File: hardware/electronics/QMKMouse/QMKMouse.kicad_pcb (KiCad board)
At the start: 4 copper layers, 104.6 x 65.8 mm, 117 parts

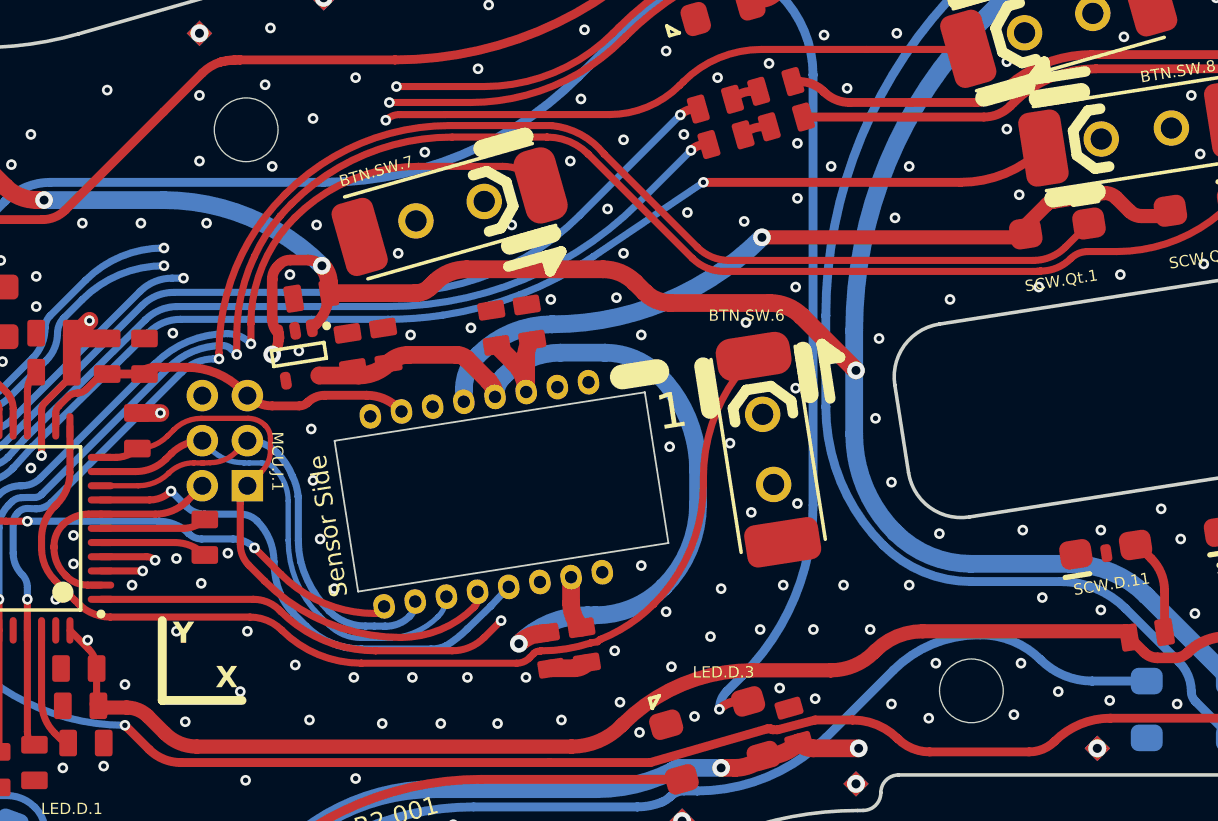
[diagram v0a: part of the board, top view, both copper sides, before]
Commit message: update schematic from PCB; sync netlist and fix some symbol orientations; also fix LED symbol
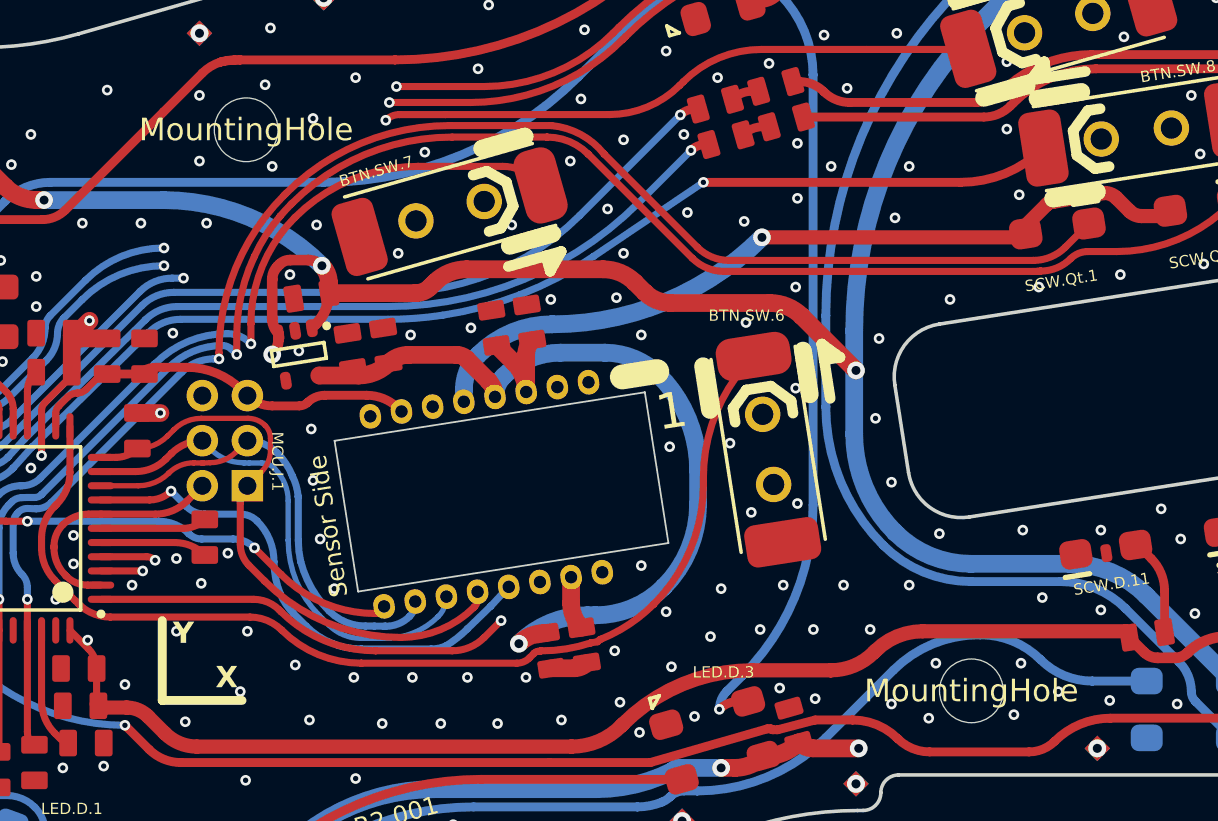
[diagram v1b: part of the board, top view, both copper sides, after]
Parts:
- BTN.SW.7, BTN.SW.8: value D2LS-21 -> SW_DIP_x01
- HOLE.1, HOLE.2: value (none) -> MountingHole
- LED.C.20, LED.C.21, LED.C.23, LED.C.24, LED.C.25, LED.C.26, LED.C.27, LED.C.28, MCU.C.22, MCU.C.4, MCU.C.5, MCU.C.6, MCU.C.8, MCU.C.9: value 0805 -> 0.1uF 100V
- LED.D.5: value IN-PI55TATPRPGPB -> Inolux_IN-PI554FCH
- LED.R.16, LED.R.17, LED.R.18, LED.R.19, SCW.R.2, SCW.R.4: value 0805 -> 1k 1%
- MCH.FID.1, MCH.FID.2: value IPC-7351 Fiducial 1mm -> Fiducial
- MCH.LOGO.2: value Coordinate system marker for assembly -> Coordinate_system_marker
- MCH.SP.1, MCH.SP.10, MCH.SP.11, MCH.SP.12, MCH.SP.13, MCH.SP.14, MCH.SP.15, MCH.SP.16, MCH.SP.17, MCH.SP.18, MCH.SP.19, MCH.SP.2, MCH.SP.20, MCH.SP.21, MCH.SP.22, MCH.SP.23, MCH.SP.24, MCH.SP.25, MCH.SP.26, MCH.SP.27, MCH.SP.28, MCH.SP.3, MCH.SP.4, MCH.SP.5, MCH.SP.6, MCH.SP.7, MCH.SP.8, MCH.SP.9: value Spark Gap -> Spark_gap
- MCU.C.1, REG.C.12, REG.C.14, REG.C.16, REG.C.18: value 0805 -> 1uF 25V
- MCU.C.7, MOS.C.10, MOS.C.11, REG.C.13, REG.C.17, USB.C.19: value 0805 -> 10uF 25V
- MCU.J.4: value HEADER2 -> Conn_01x02
- MCU.R.1, MCU.R.20, MOS.R.5, USB.R.12, USB.R.13, USB.R.14, USB.R.15, USB.R.8, USB.R.9: value 0805 -> 10k 1%
- MCU.U.1: value ATMEGA32U4RC-AU -> ATmega32U4RC-A
- MCU.Y.1: value LFXTAL055663BULK -> 8MHz
- MOS.R.3, MOS.R.4, USB.R.6, USB.R.7: value 0805 -> 22R 1%
- REG.C.15: value 0805 -> 100pF 100V
- SCW.D.11, SCW.D.12: value IR12-21C/TR8 or VSMB10940 -> IR12-21C/TR8 or VSMB10940
- SCW.R.1, SCW.R.3: value 0805 -> 100 1%
- USB.FB.4: value ACML-0805-601-T -> ACML-0805-601-T Ferrite Bead 600Ohm
- USB.R.10, USB.R.11: value 0805 -> 100R 1%
- USB.Z.1: value IP4220CZ6,125 -> IP4220CZ6
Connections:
- net NetLED.D.1_2 renamed Net-(LED.D.1-Pad2)
- net NetLED.D.1_4 renamed Net-(LED.D.1-Pad4)
- net NetLED.D.2_2 renamed Net-(LED.D.2-Pad2)
- net NetLED.D.2_4 renamed Net-(LED.D.2-Pad4)
- net NetLED.D.3_2 renamed Net-(LED.D.3-Pad2)
- net NetLED.D.4_2 renamed Net-(LED.D.4-Pad2)
- net NetLED.D.5_2 renamed Net-(LED.D.5-Pad2)
- net NetLED.D.6_2 renamed Net-(LED.D.6-Pad2)
- net NetLED.D.7_2 renamed Net-(LED.D.7-Pad2)
- net NetLED.D.8_2 renamed Net-(LED.D.8-Pad2)
- net NetMCU.C.4_2 renamed Net-(MCU.C.4-Pad2)
- net NetMCU.J.4_1 renamed Net-(MCU.J.4-Pad1)
- net NetMCU.U.1_16 renamed Net-(MCU.U.1-Pad16)
- net NetMCU.U.1_17 renamed Net-(MCU.U.1-Pad17)
- net NetMCU.U.1_18 renamed SCL
- net NetMCU.U.1_19 renamed SDA
- net NetMCU.U.1_21 renamed MOTION
- net NetMCU.U.1_3 renamed D-
- net NetMCU.U.1_4 renamed D+
- net NetMOS.C.10_2 renamed Net-(MOS.C.10-Pad2)
- net NetMOS.R.3_1 renamed Net-(MOS.R.3-Pad1)
- net NetMOS.R.4_1 renamed Net-(MOS.R.4-Pad1)
- net NetREG.C.15_2 renamed Net-(REG.C.15-Pad2)
- net NetUSB.FB.2_1 renamed Net-(USB.FB.2-Pad1)
- net NetUSB.FB.2_2 renamed Net-(USB.FB.2-Pad2)
- net NetUSB.FB.3_1 renamed Net-(USB.FB.3-Pad1)
- net NetUSB.FB.3_2 renamed Net-(USB.FB.3-Pad2)
- net NetUSB.FB.4_1 renamed Net-(USB.FB.4-Pad1)
- net NetUSB.FB.4_2 renamed Net-(USB.FB.4-Pad2)
- net NetUSB.FB.5_1 renamed Net-(USB.FB.5-Pad1)
- net NetUSB.FB.5_2 renamed Net-(USB.FB.5-Pad2)
- net NetUSB.J.3_3 renamed Net-(USB.J.3-Pad3)
- net NetUSB.J.3_9 renamed Net-(USB.J.3-Pad9)
- net ~{CS renamed ~{CS}
- net ~{RESET renamed ~{RESET}
- BTN.SW.3 pad A: NetBTN.SW.3_A -> (no net)
- BTN.SW.3 pad B: GND -> (no net)
- BTN.SW.6 pad A: NetBTN.SW.6_A -> (no net)
- BTN.SW.6 pad B: GND -> (no net)
- BTN.SW.7 pad A: NetBTN.SW.7_A -> (no net)
- BTN.SW.7 pad B: GND -> (no net)
- LBS.SW.2 pad A: NetLBS.SW.2_A -> (no net)
- LBS.SW.2 pad B: GND -> (no net)
- LED.C.25 pad 1: GND -> unconnected-(LED.C.25-Pad1)
- LED.R.18 pad 1: (no net) -> unconnected-(LED.R.18-Pad1)
- LED.R.19 pad 1: (no net) -> unconnected-(LED.R.19-Pad1)
- MCH.SP.1 pad 1: GND -> (no net)
- MCH.SP.10 pad 1: GND -> (no net)
- MCH.SP.11 pad 1: GND -> (no net)
- MCH.SP.12 pad 1: GND -> (no net)
- MCH.SP.13 pad 1: GND -> (no net)
- MCH.SP.14 pad 1: GND -> (no net)
- MCH.SP.15 pad 1: GND -> (no net)
- MCH.SP.16 pad 1: GND -> (no net)
- MCH.SP.17 pad 1: GND -> (no net)
- MCH.SP.18 pad 1: GND -> (no net)
- MCH.SP.19 pad 1: GND -> (no net)
- MCH.SP.2 pad 1: GND -> (no net)
- MCH.SP.20 pad 1: GND -> (no net)
- MCH.SP.21 pad 1: GND -> (no net)
- MCH.SP.22 pad 1: GND -> (no net)
- MCH.SP.23 pad 1: GND -> (no net)
- MCH.SP.24 pad 1: GND -> (no net)
- MCH.SP.25 pad 1: GND -> (no net)
- MCH.SP.26 pad 1: GND -> (no net)
- MCH.SP.27 pad 1: GND -> (no net)
- MCH.SP.28 pad 1: GND -> (no net)
- MCH.SP.3 pad 1: GND -> (no net)
- MCH.SP.4 pad 1: GND -> (no net)
- MCH.SP.5 pad 1: GND -> (no net)
- MCH.SP.6 pad 1: GND -> (no net)
- MCH.SP.7 pad 1: GND -> (no net)
- MCH.SP.8 pad 1: GND -> (no net)
- MCH.SP.9 pad 1: GND -> (no net)
- MCU.C.1 pad 1: GND -> Net-(MCU.C.1-Pad1)
- MCU.C.1 pad 2: NetMCU.C.1_2 -> GND
- MCU.U.1 pad 1: NetLBS.SW.2_A -> ButtonRightClick
- MCU.U.1 pad 12: NetBTN.SW.6_A -> ButtonDPI
- MCU.U.1 pad 20: NetBTN.SW.8_A -> ButtonScrollWheel
- MCU.U.1 pad 22: (no net) -> unconnected-(MCU.U.1-Pad22)
- MCU.U.1 pad 25: NetLBS.SW.1_A -> ButtonLeftClick
- MCU.U.1 pad 27: NetBTN.SW.5_A -> ButtonForward
- MCU.U.1 pad 30: NetBTN.SW.7_A -> ButtonBack
- MCU.U.1 pad 31: NetBTN.SW.3_A -> ButtonRR
- MCU.U.1 pad 32: NetBTN.SW.4_A -> ButtonLL
- MCU.U.1 pad 39: NetMCU.U.1_39 -> TopScrollWheelOpto1
- MCU.U.1 pad 41: NetMCU.U.1_41 -> TopScrollWheelOpto0
- MCU.U.1 pad 6: NetMCU.C.1_2 -> Net-(MCU.C.1-Pad1)
- MOS.U.2 pad 1: (no net) -> unconnected-(MOS.U.2-Pad1)
- MOS.U.2 pad 14: (no net) -> unconnected-(MOS.U.2-Pad14)
- MOS.U.2 pad 16: (no net) -> unconnected-(MOS.U.2-Pad16)
- MOS.U.2 pad 2: (no net) -> unconnected-(MOS.U.2-Pad2)
- MOS.U.2 pad 6: (no net) -> unconnected-(MOS.U.2-Pad6)
- REG.U.4 pad 4: (no net) -> unconnected-(REG.U.4-Pad4)
- SCW.R.1 pad 1: NetSCW.D.11_A -> Net-(SCW.D.11-Pad2)
- SCW.R.2 pad 2: NetMCU.U.1_41 -> TopScrollWheelOpto0
- SCW.R.3 pad 1: NetSCW.D.12_A -> Net-(SCW.D.12-Pad2)
- SCW.R.4 pad 2: NetMCU.U.1_39 -> TopScrollWheelOpto1
- USB.FB.1 pad 1: NetUSB.FB.1_1 -> Net-(USB.FB.1-Pad1)
- USB.J.2 pad 1: NetUSB.FB.1_1 -> Net-(USB.FB.1-Pad1)
- USB.J.3 pad 10: (no net) -> unconnected-(USB.J.3-Pad10)
- USB.J.3 pad 11: NetUSB.FB.1_1 -> (no net)
- USB.J.3 pad 12: GND -> Net-(USB.FB.1-Pad1)
- USB.J.3 pad 2: NetUSB.FB.1_1 -> Net-(USB.FB.1-Pad1)
- USB.J.3 pad 4: (no net) -> unconnected-(USB.J.3-Pad4)
- USB.R.8 pad 2: NetUSB.FB.1_1 -> Net-(USB.FB.1-Pad1)
- USB.R.9 pad 2: NetUSB.FB.1_1 -> Net-(USB.FB.1-Pad1)
- USB.Z.1 pad 5: NetUSB.FB.1_1 -> Net-(USB.FB.1-Pad1)
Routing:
- net NetBTN.SW.4_A: track 106.9 -> 0.00 mm, vias 3 -> 0
- net ButtonLL: track 0.00 -> 106.9 mm, vias 0 -> 3
- net NetBTN.SW.3_A: track 101.5 -> 0.00 mm, vias 2 -> 0
- net ButtonRR: track 0.00 -> 101.5 mm, vias 0 -> 2
- net NetLBS.SW.1_A: track 101.3 -> 0.00 mm, vias 3 -> 0
- net ButtonLeftClick: track 0.00 -> 101.3 mm, vias 0 -> 3
- net TopScrollWheelOpto1: track 0.00 -> 97.4 mm, vias 0 -> 2
- net NetMCU.U.1_39: track 97.4 -> 0.00 mm, vias 2 -> 0
- net NetLBS.SW.2_A: track 89.6 -> 0.00 mm, vias 2 -> 0
- net ButtonRightClick: track 0.00 -> 89.6 mm, vias 0 -> 2
- net TopScrollWheelOpto0: track 0.00 -> 88.2 mm, vias 0 -> 2
- net NetMCU.U.1_41: track 88.2 -> 0.00 mm, vias 2 -> 0
- net NetBTN.SW.5_A: track 71.7 -> 0.00 mm, vias 3 -> 0
- net ButtonForward: track 0.00 -> 71.7 mm, vias 0 -> 3
- net NetBTN.SW.8_A: track 70.2 -> 0.00 mm, vias 2 -> 0
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
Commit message: Fix some schematic PCB mismatch
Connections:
- MCH.SP.1 pad 1: (no net) -> GND
- MCH.SP.10 pad 1: (no net) -> GND
- MCH.SP.11 pad 1: (no net) -> GND
- MCH.SP.12 pad 1: (no net) -> GND
- MCH.SP.13 pad 1: (no net) -> GND
- MCH.SP.14 pad 1: (no net) -> GND
- MCH.SP.15 pad 1: (no net) -> GND
- MCH.SP.16 pad 1: (no net) -> GND
- MCH.SP.17 pad 1: (no net) -> GND
- MCH.SP.18 pad 1: (no net) -> GND
- MCH.SP.19 pad 1: (no net) -> GND
- MCH.SP.2 pad 1: (no net) -> GND
- MCH.SP.20 pad 1: (no net) -> GND
- MCH.SP.21 pad 1: (no net) -> GND
- MCH.SP.22 pad 1: (no net) -> GND
- MCH.SP.23 pad 1: (no net) -> GND
- MCH.SP.24 pad 1: (no net) -> GND
- MCH.SP.25 pad 1: (no net) -> GND
- MCH.SP.26 pad 1: (no net) -> GND
- MCH.SP.27 pad 1: (no net) -> GND
- MCH.SP.28 pad 1: (no net) -> GND
- MCH.SP.3 pad 1: (no net) -> GND
- MCH.SP.4 pad 1: (no net) -> GND
- MCH.SP.5 pad 1: (no net) -> GND
- MCH.SP.6 pad 1: (no net) -> GND
- MCH.SP.7 pad 1: (no net) -> GND
- MCH.SP.8 pad 1: (no net) -> GND
- MCH.SP.9 pad 1: (no net) -> GND
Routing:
- net Net-(MCU.C.1-Pad1): track 6.03 -> 12.0 mm
- net GND: track 9.25 -> 3.27 mm

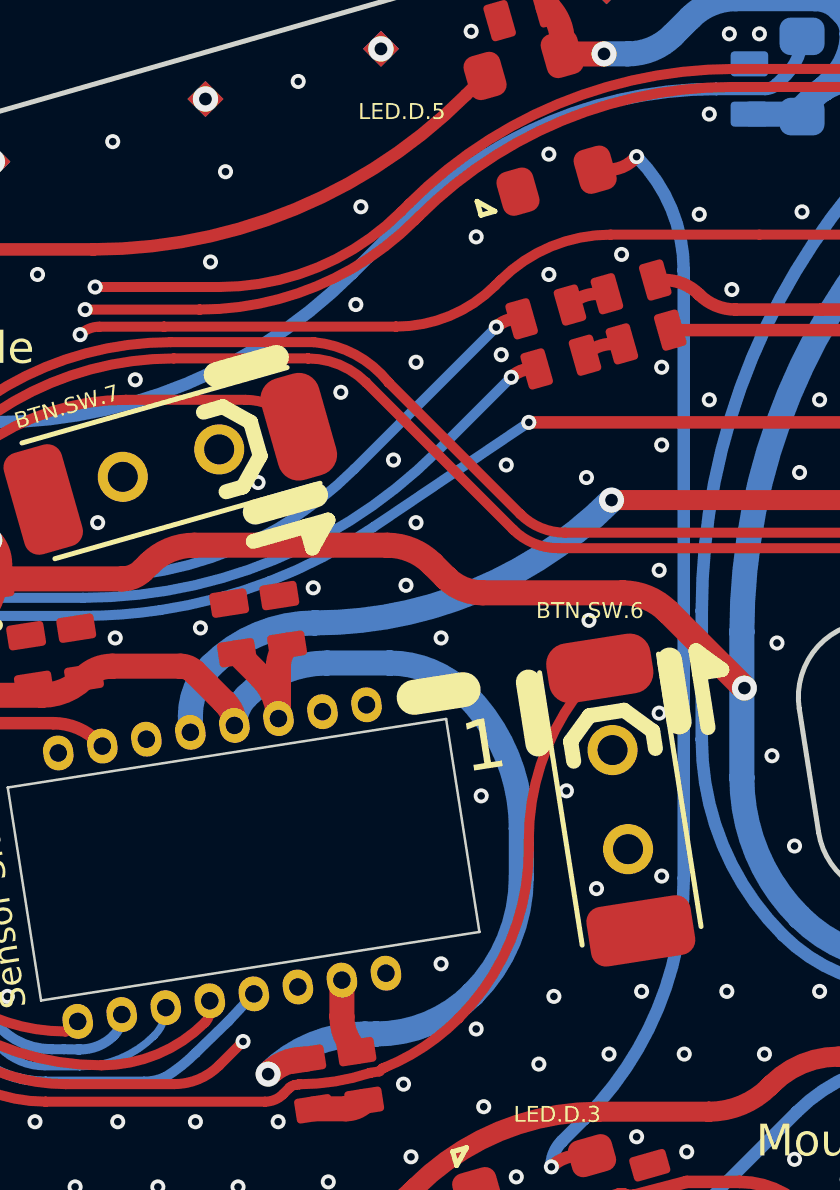
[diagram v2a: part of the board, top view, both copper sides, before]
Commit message: Fix all remaining DRC errors and schematic mismatches
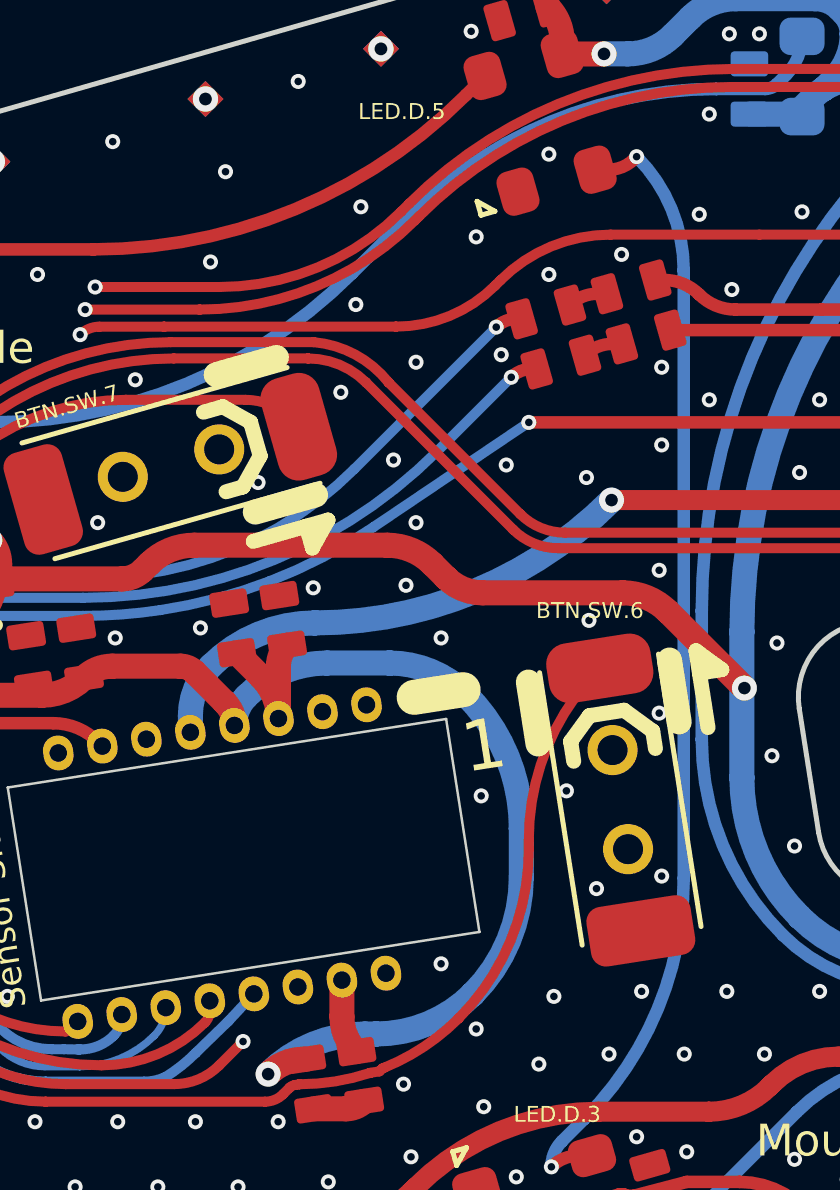
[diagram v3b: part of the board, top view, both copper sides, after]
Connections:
- MCH.FID.1 pad 1: (no net) -> unconnected-(MCH.FID.1-Pad1)
- MCH.FID.2 pad 1: (no net) -> unconnected-(MCH.FID.2-Pad1)
- MCU.C.1 pad 1: Net-(MCU.C.1-Pad1) -> GND
- MCU.C.1 pad 2: GND -> Net-(MCU.C.1-Pad2)
- MCU.U.1 pad 6: Net-(MCU.C.1-Pad1) -> Net-(MCU.C.1-Pad2)
- USB.J.3 pad 11: (no net) -> Net-(USB.FB.1-Pad1)
- USB.J.3 pad 12: Net-(USB.FB.1-Pad1) -> GND
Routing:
- net Net-(MCU.C.1-Pad1): track 12.0 -> 0.00 mm
- net GND: track 3.27 -> 9.30 mm
- net Net-(MCU.C.1-Pad2): track 0.00 -> 5.98 mm

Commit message: fix last sync errors
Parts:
- SCW.D.11, SCW.D.12: footprint LEDs.PcbLib:IR12-21C/TR8 -> LEDs.PcbLib:IR12-21C-TR8
- SCW.Qt.1, SCW.Qt.2: footprint OptoElectronics.PcbLib:PT26-51B/TR8 -> OptoElectronics.PcbLib:PT26-51B-TR8
- turned SCW.D.12 to -81.113 degrees
- turned SCW.Qt.2 to 98.887 degrees
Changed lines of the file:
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@@
     )
   )
-  (footprint "LEDs.PcbLib:IR12-21C{slash}TR8" (layer "F.Cu")
-    (at 179.239409 111.783457 -81.1130838)
+  (footprint "LEDs.PcbLib:IR12-21C-TR8" (layer "F.Cu")
+    (at 179.239409 111.783457 -81.113)
     (property "Sheetfile" "ScrollWheel-SchDoc.kicad_sch")
     (property "Sheetname" "SCW")
-    (fp_text reference "SCW.D.12" (at 2.405868 2.284283 8.8869162 unlocked) (layer "F.SilkS")
-      (effects (font (size 0.635 0.635) (thickness 0.254)) (justify left bottom))
-    )
-    (fp_text value "IR12-21C/TR8 or VSMB10940 " (at 6.000048 1.491927 unlocked) (layer "F.SilkS") hide
+    (fp_text reference "SCW.D.12" (at 2.405868 2.284283 8.887 unlocked) (layer "F.SilkS")
+      (effects (font (size 0.635 0.635) (thickness 0.254)) (justify left bottom))
+    )
+    (fp_text value "IR12-21C/TR8 or VSMB10940 " (at 6.000048 1.491927 8.38e-05 unlocked) (layer "F.SilkS") hide
       (effects (font (size 0.762 0.762) (thickness 0.254)) (justify left bottom))
     )
@@
     (fp_line (start -2.3 1.499999) (end 0.2 1.499999) (layer "B.Fab") (width 0.1))
     (fp_line (start 0.2 1.499999) (end 0.2 -1.5) (layer "B.Fab") (width 0.1))
-    (pad "" smd roundrect locked (at 0.200003 -0.002399 278.8869162) (size 1 0.6) (layers "F.Cu" "F.Paste" "F.Mask") (roundrect_rratio 0.35)
+    (pad "" smd roundrect locked (at 0.200003 -0.002399 278.887) (size 1 0.6) (layers "F.Cu" "F.Paste" "F.Mask") (roundrect_rratio 0.35)
       (solder_paste_margin -99))
-    (pad "1" smd roundrect locked (at 0 1.702397 278.8869162) (size 1.6 1.8) (layers "F.Cu" "F.Paste" "F.Mask") (roundrect_rratio 0.3)
+    (pad "1" smd roundrect locked (at 0 1.702397 278.887) (size 1.6 1.8) (layers "F.Cu" "F.Paste" "F.Mask") (roundrect_rratio 0.3)
       (net 8 "GND") (pinfunction "K") (pintype "passive") (solder_paste_margin -0.03))
-    (pad "2" smd roundrect locked (at 0.000001 -1.702399 278.8869162) (size 1.6 1.8) (layers "F.Cu" "F.Paste" "F.Mask") (roundrect_rratio 0.3)
+    (pad "2" smd roundrect locked (at 0.000001 -1.702399 278.887) (size 1.6 1.8) (layers "F.Cu" "F.Paste" "F.Mask") (roundrect_rratio 0.3)
       (net 35 "Net-(SCW.D.12-Pad2)") (pinfunction "A") (pintype "passive") (solder_paste_margin -0.03))
     (model "${KIPRJMOD}/ALTIUM_EMBEDDED_MODELS/XZxx56x-1.step"
@@
       (net 8 "GND") (pintype "input") (solder_mask_margin 0.1016) (solder_paste_margin -2.5146))
   )
-  (footprint "OptoElectronics.PcbLib:PT26-51B{slash}TR8" (layer "F.Cu")
-    (at 176.514403 93.683425 98.8869162)
+  (footprint "OptoElectronics.PcbLib:PT26-51B-TR8" (layer "F.Cu")
+    (at 176.514403 93.683425 98.887)
     (property "Sheetfile" "ScrollWheel-SchDoc.kicad_sch")
     (property "Sheetname" "SCW")
-    (fp_text reference "SCW.Qt.2" (at -3.298956 -2.338244 8.8869162 unlocked) (layer "F.SilkS")
-      (effects (font (size 0.635 0.635) (thickness 0.254)) (justify left bottom))
-    )
-    (fp_text value "PT26-51B/TR8 or PT12-21B/TR8" (at -3.871855 -2.77779 unlocked) (layer "F.SilkS") hide
+    (fp_text reference "SCW.Qt.2" (at -3.298956 -2.338244 8.887 unlocked) (layer "F.SilkS")
+      (effects (font (size 0.635 0.635) (thickness 0.254)) (justify left bottom))
+    )
+    (fp_text value "PT26-51B/TR8 or PT12-21B/TR8" (at -3.871855 -2.77779 8.38e-05 unlocked) (layer "F.SilkS") hide
       (effects (font (size 0.762 0.762) (thickness 0.254)) (justify left bottom))
     )
@@
     (fp_line (start 0.499999 1.6) (end -2.100007 1.599999) (layer "B.Fab") (width 0.1))
     (fp_line (start 0.5 -1.599999) (end 0.499999 1.6) (layer "B.Fab") (width 0.1))
-    (pad "1" smd roundrect locked (at 0.000001 -1.802398 98.8869162) (size 1.7 1.8) (layers "F.Cu" "F.Paste" "F.Mask") (roundrect_rratio 0.3)
+    (pad "1" smd roundrect locked (at 0.000001 -1.802398 98.887) (size 1.7 1.8) (layers "F.Cu" "F.Paste" "F.Mask") (roundrect_rratio 0.3)
       (net 7 "3V3") (pinfunction "C") (pintype "passive") (solder_paste_margin -0.03))
-    (pad "2" smd roundrect locked (at 0 1.802396 98.8869162) (size 1.7 1.8) (layers "F.Cu" "F.Paste" "F.Mask") (roundrect_rratio 0.3)
+    (pad "2" smd roundrect locked (at 0 1.802396 98.887) (size 1.7 1.8) (layers "F.Cu" "F.Paste" "F.Mask") (roundrect_rratio 0.3)
       (net 36 "TopScrollWheelOpto1") (pinfunction "E") (pintype "passive") (solder_paste_margin -0.03))
     (model "${KIPRJMOD}/ALTIUM_EMBEDDED_MODELS/PT26-51B-TR8.stp"
@@
       (net 6 "1V8") (pinfunction "VOUT") (pintype "power_out") (solder_paste_margin -0.04))
   )
-  (footprint "LEDs.PcbLib:IR12-21C{slash}TR8" (layer "F.Cu")
+  (footprint "LEDs.PcbLib:IR12-21C-TR8" (layer "F.Cu")
     (at 171.089402 113.05844 -81.1130838)
     (property "Sheetfile" "ScrollWheel-SchDoc.kicad_sch")
@@
       (net 8 "GND") (pintype "input") (solder_mask_margin 0.1016) (solder_paste_margin -2.5146))
   )
-  (footprint "OptoElectronics.PcbLib:PT26-51B{slash}TR8" (layer "F.Cu")
+  (footprint "OptoElectronics.PcbLib:PT26-51B-TR8" (layer "F.Cu")
     (at 168.364404 94.958474 98.8869162)
     (property "Sheetfile" "ScrollWheel-SchDoc.kicad_sch")

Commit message: fix ground connection of LED
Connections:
- LED.C.25 pad 1: unconnected-(LED.C.25-Pad1) -> GND
